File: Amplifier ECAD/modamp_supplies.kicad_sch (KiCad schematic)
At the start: 11 parts, among them U1 MCP6004, U2 MCP6004, U3 MCP6004, U4 Teensy 4.1

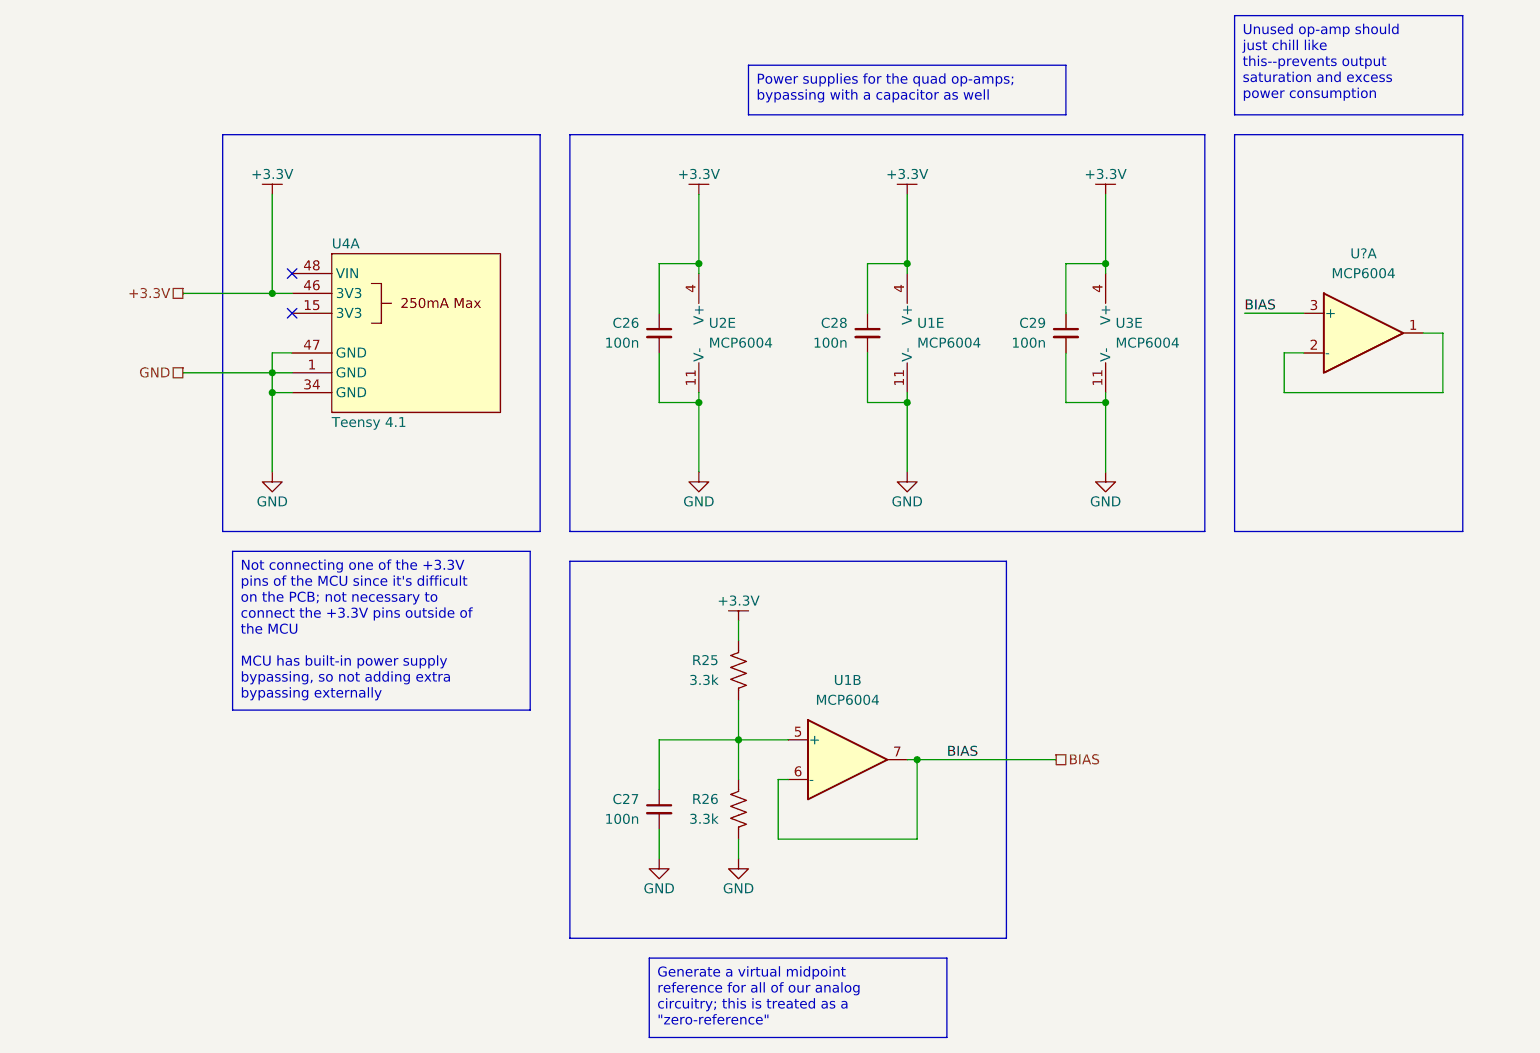
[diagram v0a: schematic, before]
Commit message: File renaming; updating supplier references
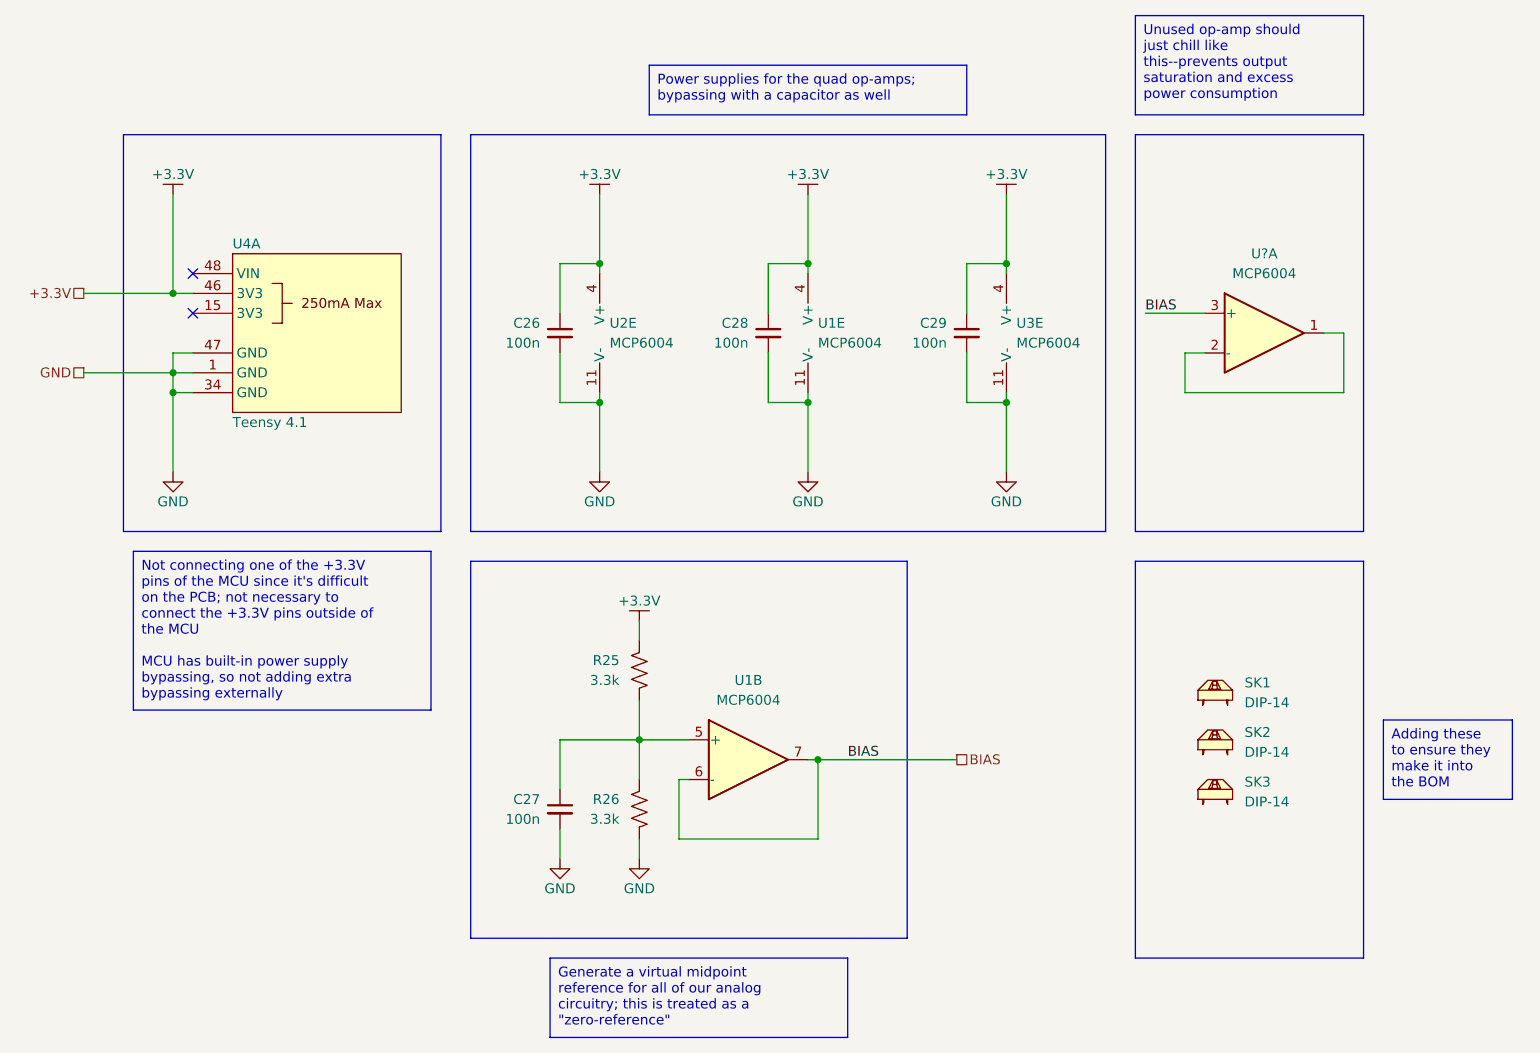
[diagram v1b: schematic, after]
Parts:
- added SK1, SK2, SK3: DIP-14, symbol Custom-Connector:ICS-314-T
- C26, C27, C28, C29: footprint Custom-RLC:C_Disc_L7.2mm_W2.5mm_H6.6mm_P5.00mm_MODIFIED_1 -> Custom-RLC:C_KEMET_C317; symbol Custom-CapacitorTHT:FG28X7R1H104KNT06 -> Custom-CapacitorTHT:C317C104K5R5TA; Manufacturer TDK Corporation -> KEMET; Part Number FG28X7R1H104KNT06 -> C317C104K5R5TA
- R25, R26: symbol Custom-ResistorTHT:MFR-25FRF52-3K3 -> Custom-ResistorTHT:CF14JT3K30; Manufacturer YAGEO -> Stackpole Electronics Inc; Part Number MFR-25FRF52-3K3 -> CF14JT3K30
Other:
- moved on the sheet: C26, C27, C28, C29, R25, R26, U1B, U1E, U2E, U3E, U4A, U?A
